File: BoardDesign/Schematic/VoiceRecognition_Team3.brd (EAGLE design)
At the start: 106.7 x 63.5 mm, 52 parts, among them J1 5.5x2.1mm Barrel, Q1 16MHz, X1 USB-A

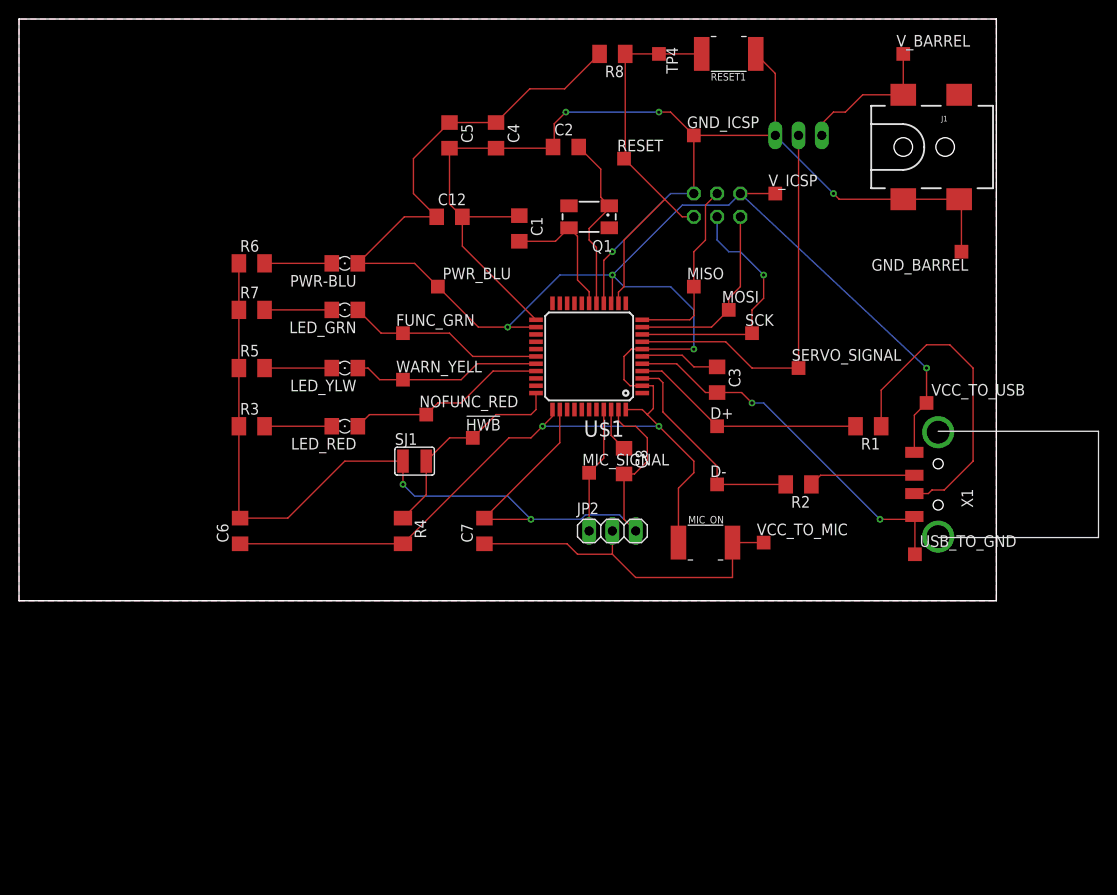
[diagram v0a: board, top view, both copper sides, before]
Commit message: Added Updated Board and BOM, note this will not be the final revision
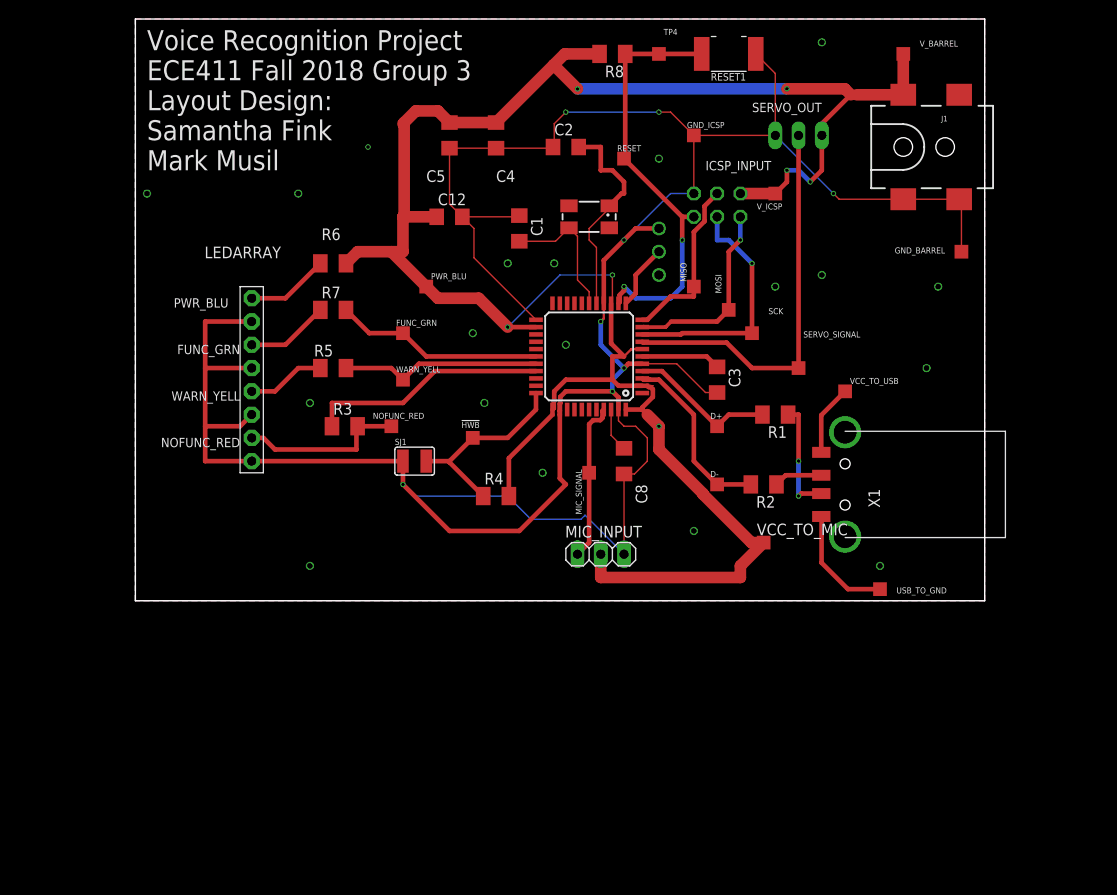
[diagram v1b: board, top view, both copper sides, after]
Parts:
- removed C6: 100nF, rcl:C1206
- removed C7: 10uF, rcl:C1206
- removed JP2: (no value), pinhead:1X03
- removed LED_GRN, LED_RED, LED_YLW, PWR-BLU: (no value), led:1206
- removed MIC_ON: (no value), adafruit:BTN_CK_KSS
- added LEDARRAY: (no value), adafruit:1X08-BIG
- added LOCK_RESET: (no value), adafruit:1X03
- added MIC_INPUT: (no value), pinhead:1X03
- moved R4 10.9 mm to (52.1, 11.4), turned to 0 degrees
- moved R1 10.2 mm to (82.5, 20.3)
- moved R3 10.2 mm to (35.6, 19.1)
- moved X1 10.2 mm to (90.2, 12.7)
- moved VCC_TO_USB 8.98 mm to (90.2, 22.9)
- moved R5 8.89 mm to (34.3, 25.4), turned to 180 degrees
- moved R6 8.89 mm to (34.3, 36.8)
- moved R7 8.89 mm to (34.3, 31.8)
- moved USB_TO_GND 5.39 mm to (94.0, 1.27)
- moved NOFUNC_RED 4.02 mm to (40.6, 19.1)
- moved R2 3.81 mm to (81.3, 12.7)
- moved PWR_BLU 1.27 mm to (44.5, 34.3)
- renumbered JP1 to ICSP_INPUT, JP3 to SERVO_OUT
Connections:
- net N$13 renamed MOSI
- net N$17 renamed MISO
- net N$2 renamed SCK
- removed net N$15: C7.1, JP2.2, MIC_ON.P$2, VCC_TO_MIC.TP
- removed net N$8: LED_RED.C, R3.2
- removed net SERVO_POS: J1.VIN0, SERVO_OUT.1, V_BARREL.TP
- new net LOCK_RESET: LOCK_RESET.2, U$1.12
- new net N$2: USB_TO_GND.TP, X1.4
- new net N$4: LEDARRAY.1, R6.1
- net FUNC_GRN: now also LEDARRAY.3, R7.1, R7.2; no longer LED_GRN.A
- net GND: now also LEDARRAY.2, LEDARRAY.4, LEDARRAY.6, LEDARRAY.8, LOCK_RESET.1, MIC_INPUT.3; no longer C6.2, C7.2, JP2.3, R3.1, R5.1, R6.1, R7.1, USB_TO_GND.TP, X1.4
- net MIC_SIGNAL: now also MIC_INPUT.1; no longer JP2.1
- net N$5: now also LEDARRAY.5, R5.2; no longer PWR-BLU.C, R6.2
- net N$6: now also LEDARRAY.7, NOFUNC_RED.TP, R3.2; no longer LED_GRN.C, R7.2
- net N$7: now also VCC_TO_USB.TP, X1.1; no longer LED_YLW.C, R5.2
- net NOFUNC_RED: now also R3.1; no longer LED_RED.A, NOFUNC_RED.TP
- net VCC: now also J1.VIN0, MIC_INPUT.2, R6.2, SERVO_OUT.1, VCC_TO_MIC.TP, V_BARREL.TP; no longer C6.1, MIC_ON.P$1, PWR-BLU.A, VCC_TO_USB.TP, X1.1
- net WARN_YELL: now also R5.1; no longer LED_YLW.A
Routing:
- net N$15: track 38.4 -> 0.00 mm, vias 0 -> 1
- net N$3: track 35.1 -> 12.6 mm, vias 0 -> 2
- net SERVO_POS: track 15.9 -> 0.00 mm
- net GND: track 288.6 -> 304.3 mm
- net FUNC_GRN: track 21.6 -> 34.3 mm
- net N$2: track 0.00 -> 12.7 mm
- net N$6: track 7.34 -> 18.2 mm
- net N$12: track 25.8 -> 16.1 mm
- net N$4: track 0.00 -> 9.07 mm
- net VCC: track 246.3 -> 238.1 mm, vias 6 -> 7
- net N$8: track 7.34 -> 0.00 mm, vias 0 -> 1
- net LOCK_RESET: track 0.00 -> 7.13 mm
- net N$9: track 11.7 -> 5.30 mm
- net RST: track 43.5 -> 49.9 mm, vias 0 -> 2
- net NOFUNC_RED: track 21.9 -> 26.3 mm
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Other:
- board size 106.7 x 63.5 mm -> 92.7 x 63.5 mm
- board text added: "FUNC_GRN"
- board text added: "ICSP_INPUT"
- board text added: "NOFUNC_RED"
- board text added: "PWR_BLU"
- board text added: "SERVO_OUT"
- board text added: "Voice Recognition Project ECE411 Fall 2018 Group 3 Layout Design: Samantha Fink Mark Musil"
- board text added: "WARN_YELL"

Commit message: Added a few changes to the board per andrew's suggestion
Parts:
- added C10, C11, C6, C7, C9: 100nF, rcl:C1206
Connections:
- net GND: now also C10.2, C11.2, C6.2, C7.2, C9.2
- net VCC: now also C10.1, C11.1, C6.1, C7.1, C9.1
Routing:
- net GND: track 304.3 -> 286.4 mm
- net VCC: track 238.1 -> 230.5 mm, vias 7 -> 5
- net RST: track 49.9 -> 50.1 mm, vias 2 -> 4

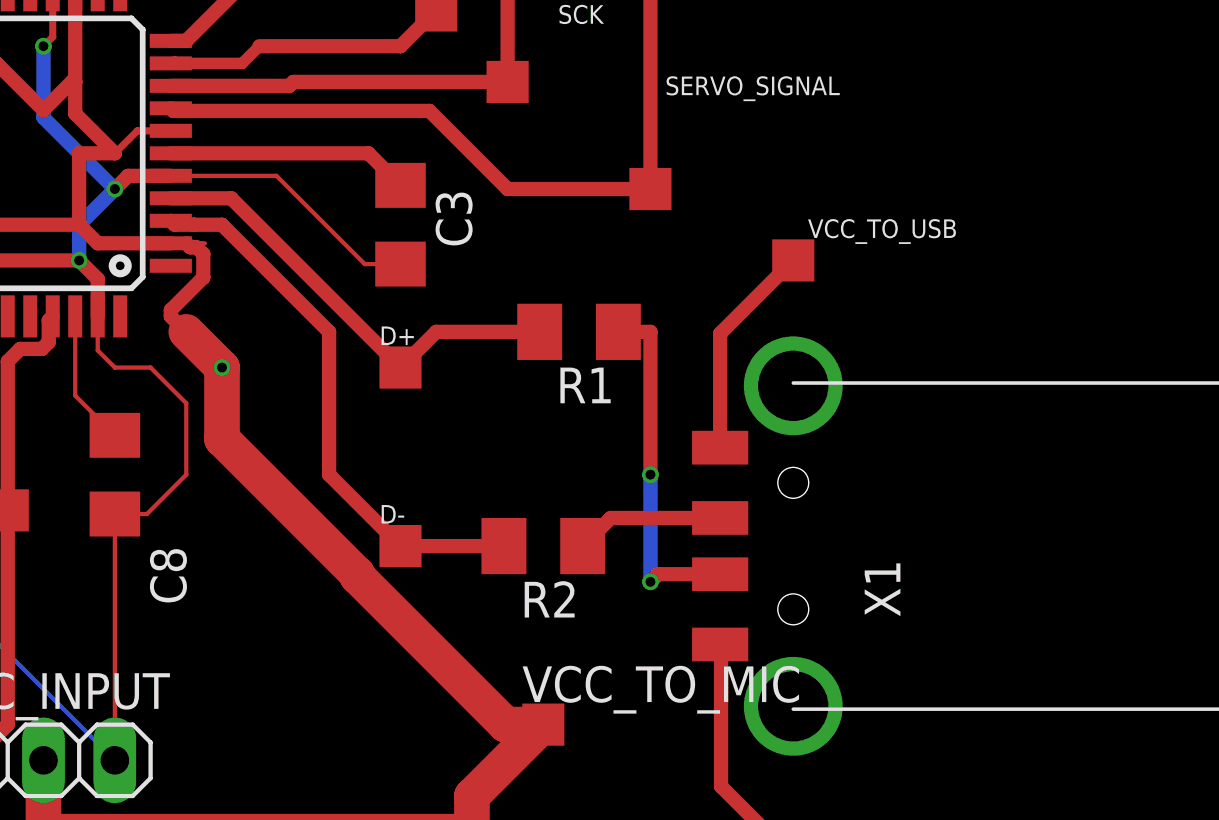
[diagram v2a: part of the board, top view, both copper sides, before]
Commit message: Added a connection to ground in the USB jack
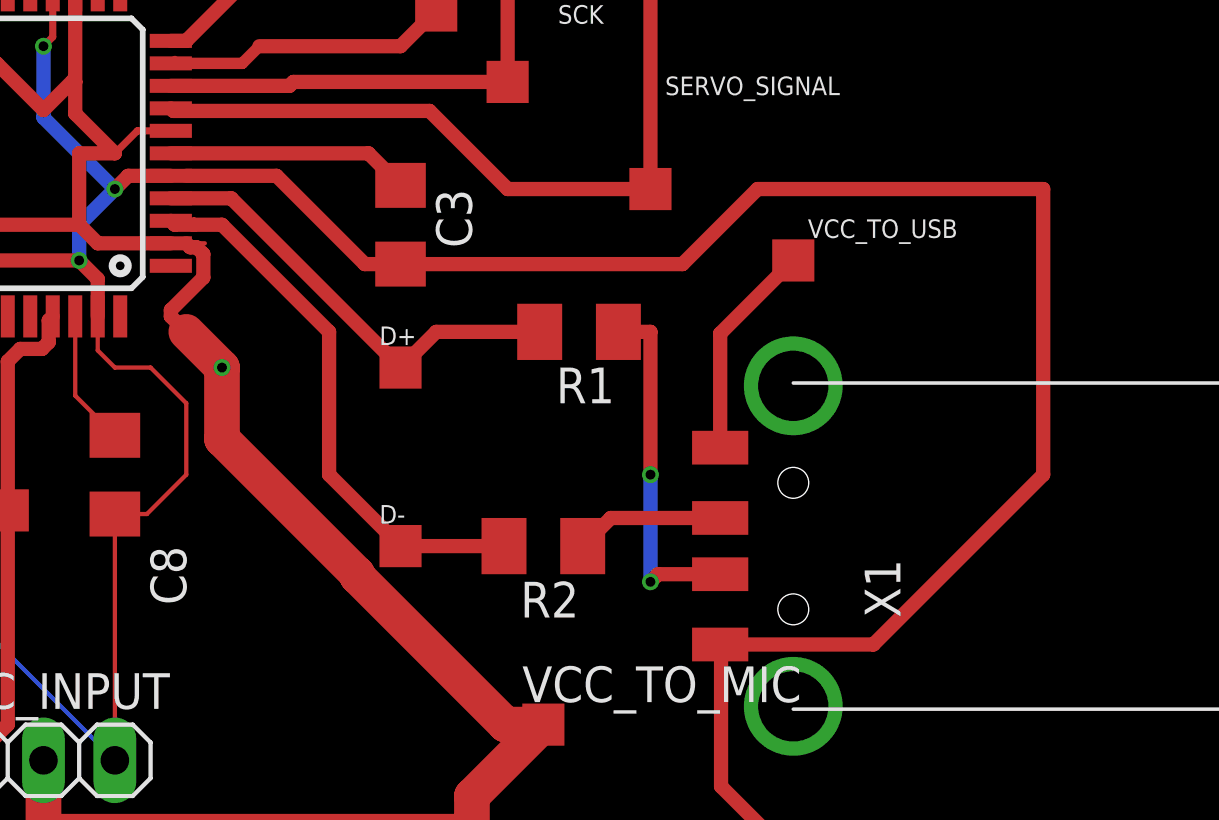
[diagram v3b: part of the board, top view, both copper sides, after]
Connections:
- removed net N$2: USB_TO_GND.TP, X1.4
- net GND: now also USB_TO_GND.TP, X1.4
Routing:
- net GND: track 286.4 -> 347.1 mm
- net N$2: track 12.7 -> 0.00 mm
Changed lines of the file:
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@@
 <wire x1="102.87" y1="38.1" x2="102.87" y2="43.58" width="0.1524" layer="1"/>
 <wire x1="102.87" y1="43.58" x2="102.62" y2="43.83" width="0.1524" layer="1"/>
-<wire x1="76.2" y1="22.73" x2="74.93" y2="22.73" width="0.1524" layer="1"/>
-<wire x1="74.93" y1="22.73" x2="71.79" y2="25.87" width="0.1524" layer="1"/>
-<wire x1="71.79" y1="25.87" x2="68.03" y2="25.87" width="0.1524" layer="1"/>
+<wire x1="68.58" y1="25.87" x2="68.03" y2="25.87" width="0.1524" layer="1"/>
 <wire x1="66.04" y1="13.84" x2="66.04" y2="5.08" width="0.1524" layer="1"/>
 <wire x1="59.03" y1="17.25" x2="59.03" y2="20.32" width="0.1524" layer="1"/>
@@
 <contactref element="C9" pad="2"/>
 <contactref element="C11" pad="2"/>
+<contactref element="X1" pad="4"/>
+<contactref element="USB_TO_GND" pad="TP"/>
+<wire x1="87.63" y1="9.14" x2="87.57" y2="9.2" width="0.1524" layer="1"/>
+<wire x1="93.98" y1="1.27" x2="90.4825" y2="1.27" width="0.508" layer="1"/>
+<wire x1="90.4825" y1="1.27" x2="87.60125" y2="4.15125" width="0.508" layer="1"/>
+<wire x1="87.60125" y1="4.15125" x2="87.60125" y2="9.11125" width="0.508" layer="1"/>
+<wire x1="87.60125" y1="9.11125" x2="87.63" y2="9.14" width="0.508" layer="1"/>
+<wire x1="87.57" y1="9.2" x2="93.02" y2="9.2" width="0.508" layer="1"/>
+<wire x1="99.06" y1="15.24" x2="99.06" y2="25.4" width="0.508" layer="1"/>
+<wire x1="99.06" y1="25.4" x2="88.9" y2="25.4" width="0.508" layer="1"/>
+<wire x1="86.23" y1="22.73" x2="76.2" y2="22.73" width="0.508" layer="1"/>
+<wire x1="93.02" y1="9.2" x2="99.06" y2="15.24" width="0.508" layer="1"/>
+<wire x1="88.9" y1="25.4" x2="86.23" y2="22.73" width="0.508" layer="1"/>
+<wire x1="76.2" y1="22.73" x2="74.93" y2="22.73" width="0.508" layer="1"/>
+<wire x1="74.93" y1="22.73" x2="71.79" y2="25.87" width="0.508" layer="1"/>
+<wire x1="71.79" y1="25.87" x2="68.58" y2="25.87" width="0.508" layer="1"/>
 <wire x1="63.5" y1="30.48" x2="56.43" y2="30.67" width="0" layer="19" extent="1-1"/>
 <wire x1="16.64" y1="-3.81" x2="20.32" y2="15.24" width="0" layer="19" extent="1-1"/>
@@
 <wire x1="68.576" y1="30.67" x2="71.12" y2="33.214" width="0.508" layer="1"/>
 </signal>
-<signal name="N$2">
-<contactref element="X1" pad="4"/>
-<contactref element="USB_TO_GND" pad="TP"/>
-<wire x1="87.63" y1="9.14" x2="87.57" y2="9.2" width="0.1524" layer="1"/>
-<wire x1="93.98" y1="1.27" x2="90.4825" y2="1.27" width="0.508" layer="1"/>
-<wire x1="90.4825" y1="1.27" x2="87.60125" y2="4.15125" width="0.508" layer="1"/>
-<wire x1="87.60125" y1="4.15125" x2="87.60125" y2="9.11125" width="0.508" layer="1"/>
-<wire x1="87.60125" y1="9.11125" x2="87.63" y2="9.14" width="0.508" layer="1"/>
-</signal>
 </signals>

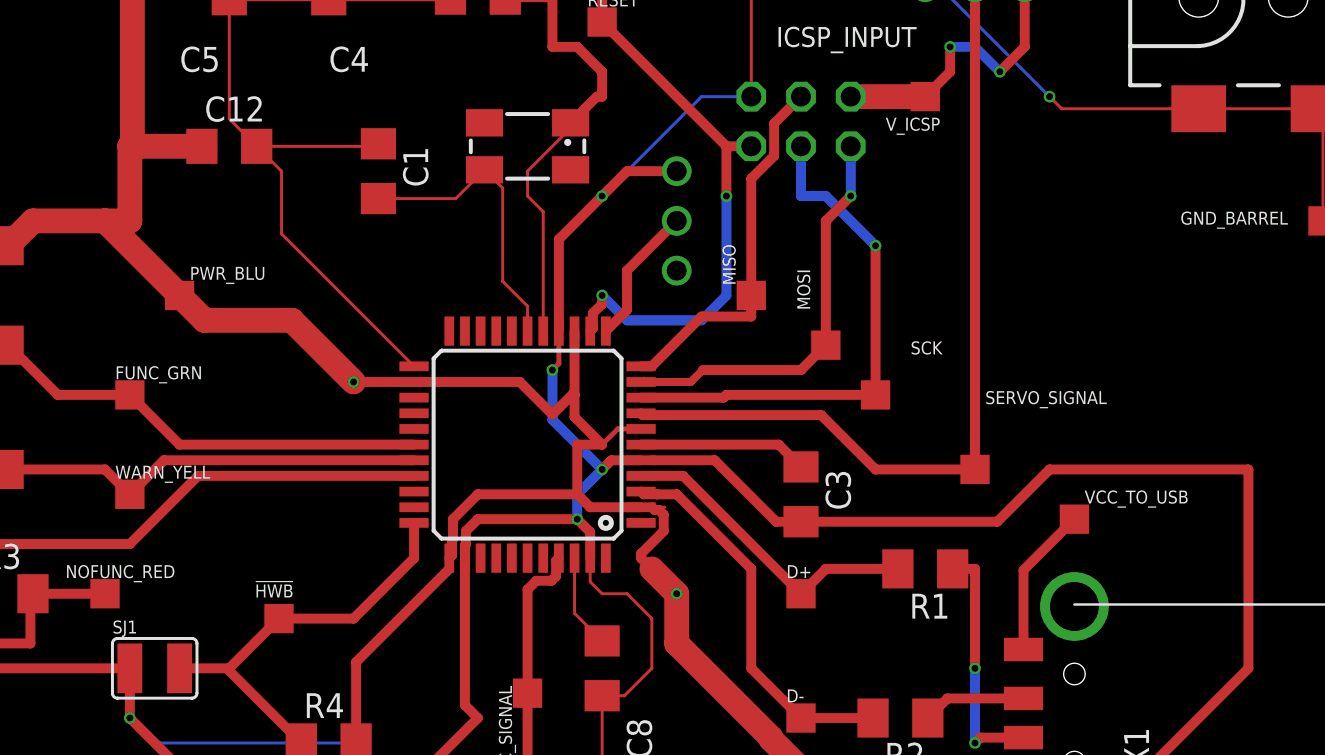
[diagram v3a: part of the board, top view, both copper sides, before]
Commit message: yeah
* rearranged bypass caps to VCC

* Added tolerances to bottom right of schem
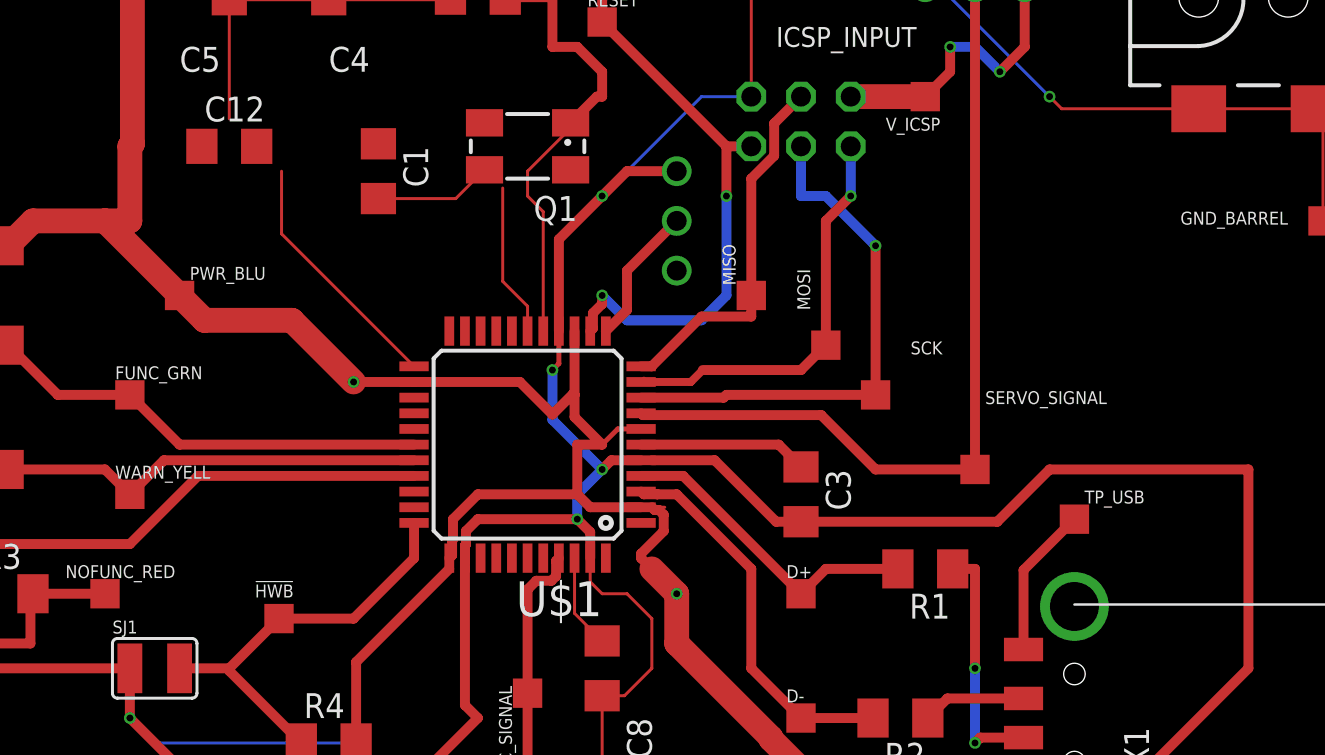
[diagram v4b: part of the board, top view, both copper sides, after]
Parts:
- renumbered VCC_TO_USB to TP_USB
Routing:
- net GND: track 347.1 -> 337.3 mm
- net VCC: track 230.5 -> 226.8 mm
- net N$2: track 15.2 -> 13.9 mm
